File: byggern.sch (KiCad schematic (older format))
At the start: 41 parts, among them U1 ATmega162-16PU

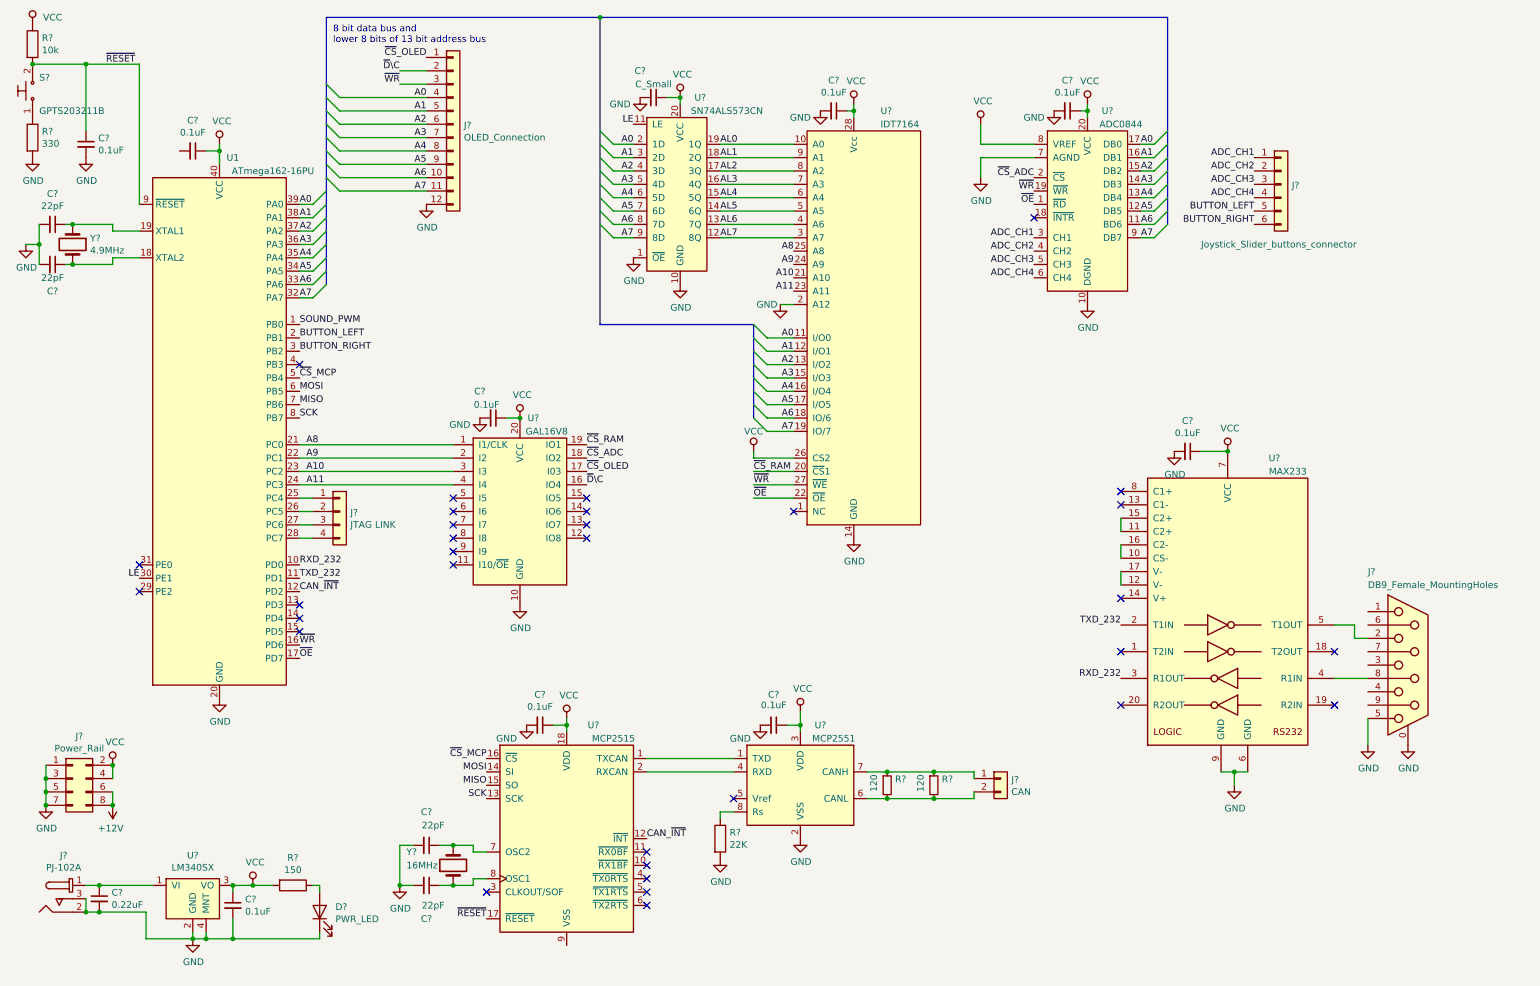
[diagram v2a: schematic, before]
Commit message: Correct warnings from electrical error check and change tri-state to output rule to ignore, no critical warnings left
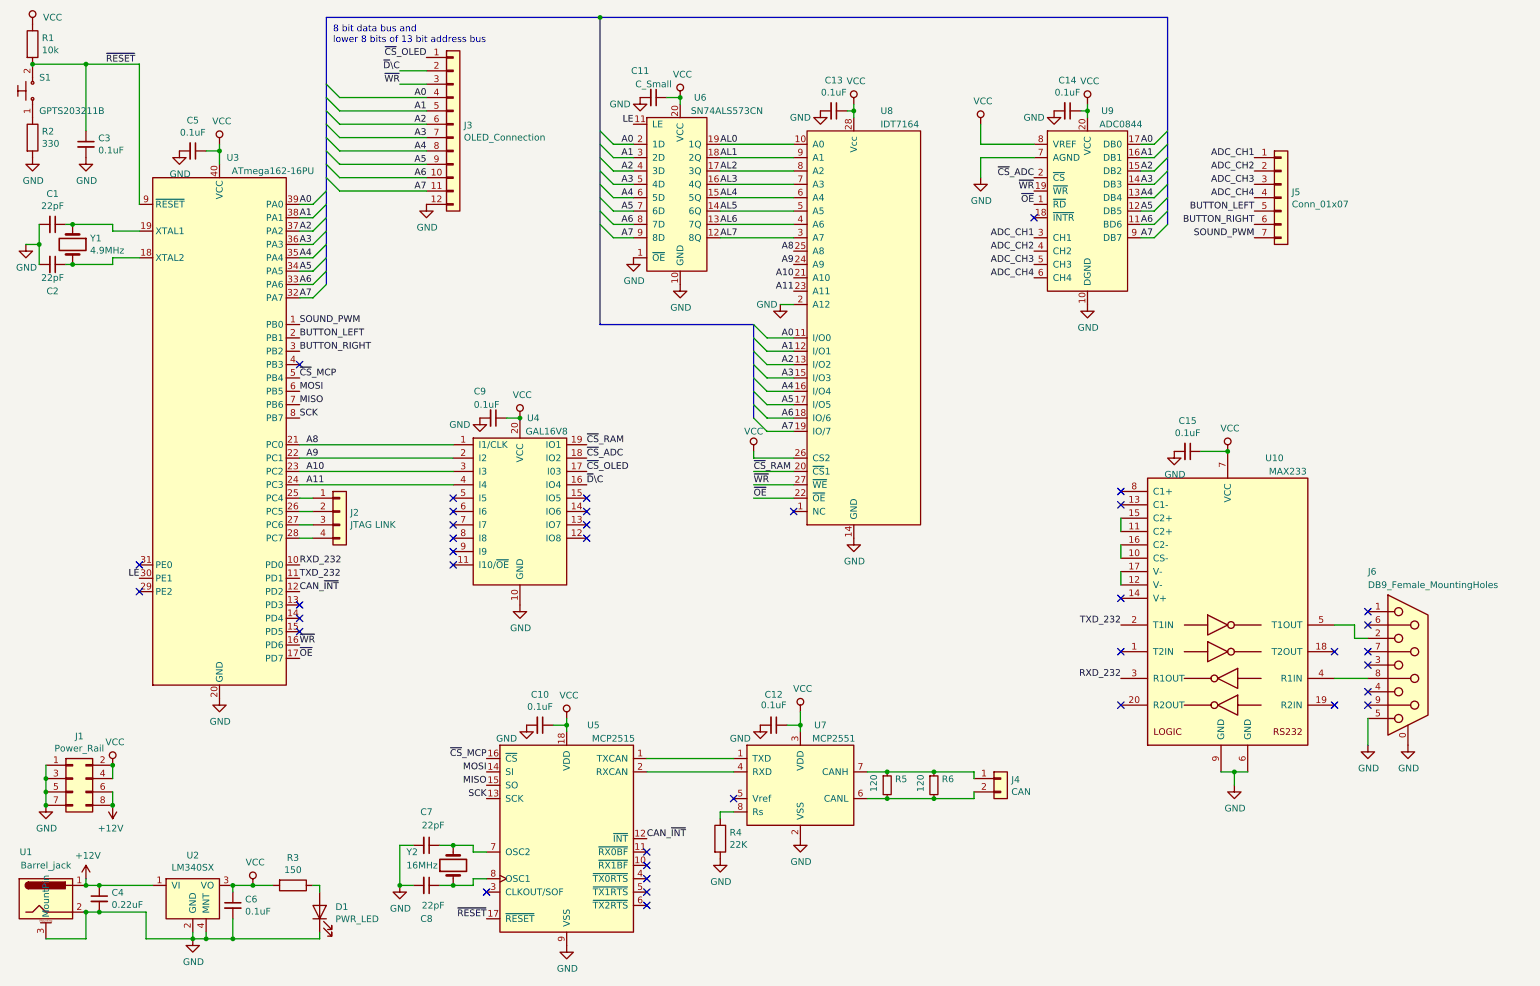
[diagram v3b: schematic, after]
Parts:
- removed J?: PJ-102A, digikey-footprints:Barrel_Jack_5.5mmODx2.1mmID_PJ-102A, symbol dk_Barrel-Power-Connectors:PJ-102A
- removed J?: Joystick_Slider_buttons_connector, symbol Connector_Generic:Conn_01x06
- added J5: Conn_01x07, symbol Connector_Generic:Conn_01x07
- added U1: Barrel_jack, symbol byggern:Barrel_jack
- gave numbers to parts that had none: 38
- renumbered U1 to U3
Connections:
- net +12V: now also C4.1, U2.1 (VI), U1.1
- net ADC_CH1: now also J5.1 (Pin_1)
- net ADC_CH2: now also J5.2 (Pin_2)
- net ADC_CH3: now also J5.3 (Pin_3)
- net ADC_CH4: now also J5.4 (Pin_4)
- net BUTTON_LEFT: now also J5.5 (Pin_5)
- net BUTTON_RIGHT: now also J5.6 (Pin_6)
- net GND: now also C5.2, U5.9 (VSS), U1.2, U1.3 (MountPin)
- net SOUND_PWM: now also J5.7 (Pin_7)
- no-connect marks 32 -> 38

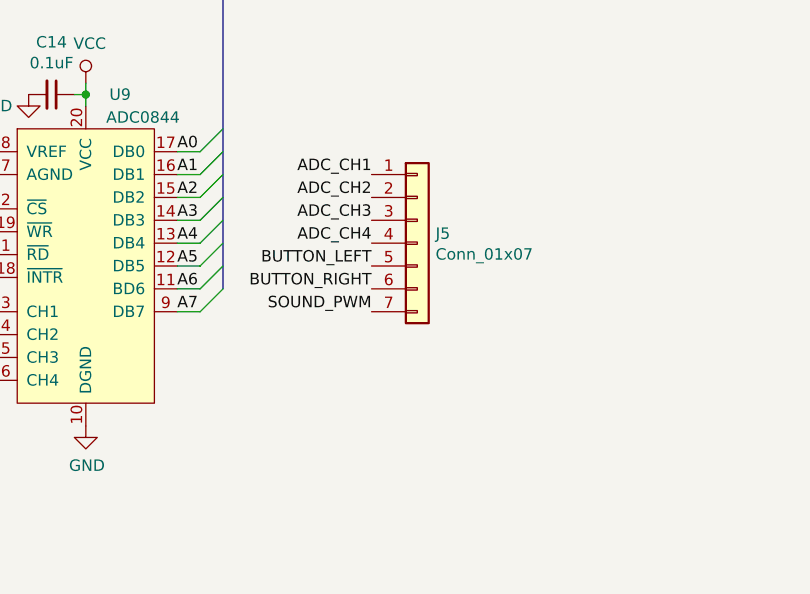
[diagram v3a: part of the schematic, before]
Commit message: Correct error in gitignore and add power to P1000-header
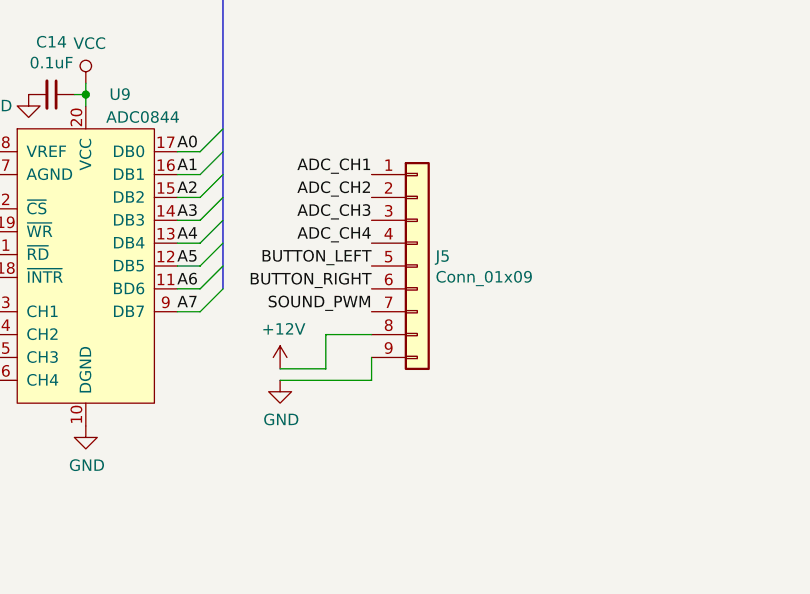
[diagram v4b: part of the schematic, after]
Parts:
- removed J5: Conn_01x07, symbol Connector_Generic:Conn_01x07
- added J5: Conn_01x09, symbol Connector_Generic:Conn_01x09
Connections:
- net +12V: now also J5.8 (Pin_8)
- net ADC_CH1: now also J5.1 (Pin_1)
- net ADC_CH2: now also J5.2 (Pin_2)
- net ADC_CH3: now also J5.3 (Pin_3)
- net ADC_CH4: now also J5.4 (Pin_4)
- net BUTTON_LEFT: now also J5.5 (Pin_5)
- net BUTTON_RIGHT: now also J5.6 (Pin_6)
- net GND: now also J5.9 (Pin_9)
- net SOUND_PWM: now also J5.7 (Pin_7)
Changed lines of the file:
@@
 	10450 5500 10700 5500
 $Comp
-L power:GND #PWR043
+L power:GND #PWR045
 U 1 1 5D9F4210
 P 10700 6000
-F 0 "#PWR043" H 10700 5750 50  0001 C CNN
+F 0 "#PWR045" H 10700 5750 50  0001 C CNN
 F 1 "GND" H 10705 5827 50  0000 C CNN
 F 2 "" H 10700 6000 50  0001 C CNN
@@
 $EndComp
 $Comp
-L power:GND #PWR044
+L power:GND #PWR046
 U 1 1 5D9F4B68
 P 11000 6000
-F 0 "#PWR044" H 11000 5750 50  0001 C CNN
+F 0 "#PWR046" H 11000 5750 50  0001 C CNN
 F 1 "GND" H 11005 5827 50  0000 C CNN
 F 2 "" H 11000 6000 50  0001 C CNN
@@
 	9700 6200 9600 6200
 $Comp
-L power:GND #PWR042
+L power:GND #PWR044
 U 1 1 5DA02D2F
 P 9700 6300
-F 0 "#PWR042" H 9700 6050 50  0001 C CNN
+F 0 "#PWR044" H 9700 6050 50  0001 C CNN
 F 1 "GND" H 9705 6127 50  0000 C CNN
 F 2 "" H 9700 6300 50  0001 C CNN
@@
 $EndComp
 $Comp
-L power:VCC #PWR041
+L power:VCC #PWR043
 U 1 1 5D9E6B36
 P 9650 3800
-F 0 "#PWR041" H 9650 3650 50  0001 C CNN
+F 0 "#PWR043" H 9650 3650 50  0001 C CNN
 F 1 "VCC" H 9667 3973 50  0000 C CNN
 F 2 "" H 9650 3800 50  0001 C CNN
@@
 	1    0    0    -1
 $EndComp
-$Comp
-L Connector_Generic:Conn_01x07 J5
-U 1 1 5DF07C49
-P 10050 1900
-F 0 "J5" H 10130 1942 50  0000 L CNN
-F 1 "Conn_01x07" H 10130 1851 50  0000 L CNN
-F 2 "" H 10050 1900 50  0001 C CNN
-F 3 "~" H 10050 1900 50  0001 C CNN
-	1    10050 1900
-	1    0    0    -1
-$EndComp
 Text Label 9850 2200 2    50   ~ 0
 SOUND_PWM
+$Comp
+L Connector_Generic:Conn_01x09 J5
+U 1 1 5D9EFB95
+P 10050 2000
+F 0 "J5" H 10130 2042 50  0000 L CNN
+F 1 "Conn_01x09" H 10130 1951 50  0000 L CNN
+F 2 "" H 10050 2000 50  0001 C CNN
+F 3 "~" H 10050 2000 50  0001 C CNN
+	1    10050 2000
+	1    0    0    -1
+$EndComp
+Wire Wire Line
+	9850 2300 9650 2300
+Wire Wire Line
+	9850 2400 9850 2500
+Wire Wire Line
+	9850 2500 9450 2500
+$Comp
+L power:GND #PWR042
+U 1 1 5DA033E3
+P 9450 2500
+F 0 "#PWR042" H 9450 2250 50  0001 C CNN
+F 1 "GND" H 9455 2327 50  0000 C CNN
+F 2 "" H 9450 2500 50  0001 C CNN
+F 3 "" H 9450 2500 50  0001 C CNN
+	1    9450 2500
+	1    0    0    -1
+$EndComp
+$Comp
+L power:+12V #PWR041
+U 1 1 5DA06A7C
+P 9450 2450
+F 0 "#PWR041" H 9450 2300 50  0001 C CNN
+F 1 "+12V" H 9465 2623 50  0000 C CNN
+F 2 "" H 9450 2450 50  0001 C CNN
+F 3 "" H 9450 2450 50  0001 C CNN
+	1    9450 2450
+	1    0    0    -1
+$EndComp
+Wire Wire Line
+	9650 2300 9650 2450
+Wire Wire Line
+	9650 2450 9450 2450
 Wire Bus Line
 	6100 2850 6100 3550

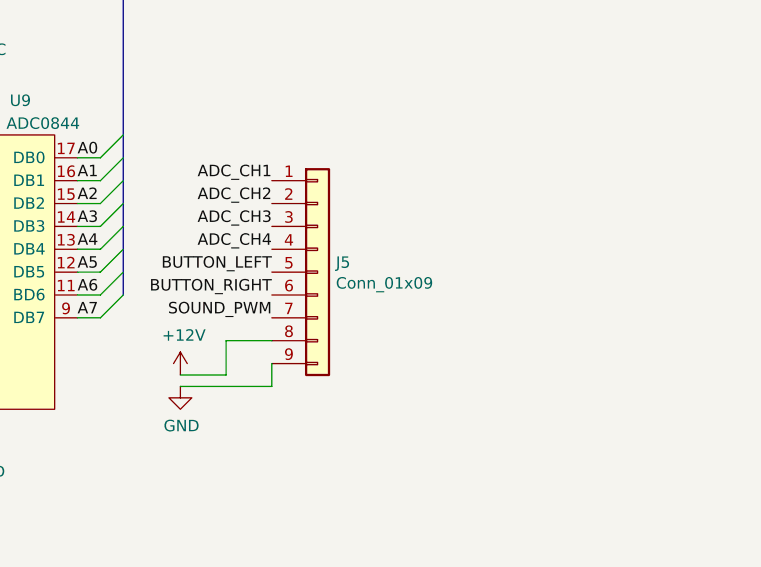
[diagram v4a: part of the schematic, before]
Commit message: Change name of P1000 Header
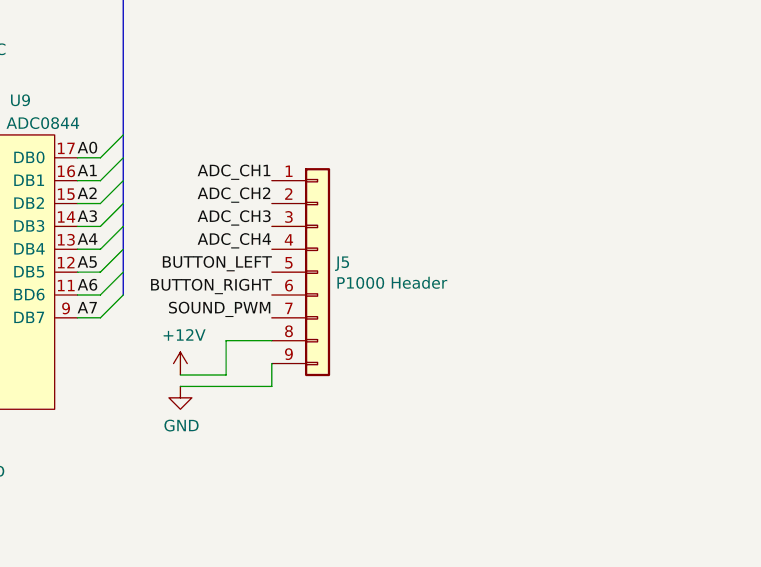
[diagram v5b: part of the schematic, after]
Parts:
- J5: value Conn_01x09 -> P1000 Header
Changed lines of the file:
@@
 P 10050 2000
 F 0 "J5" H 10130 2042 50  0000 L CNN
-F 1 "Conn_01x09" H 10130 1951 50  0000 L CNN
+F 1 "P1000 Header" H 10130 1951 50  0000 L CNN
 F 2 "" H 10050 2000 50  0001 C CNN
 F 3 "~" H 10050 2000 50  0001 C CNN

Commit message: Start assignment of footprints
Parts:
- C1, C10, C11, C12, C13, C14, C15, C2, C3, C4, C5, C6, C7, C8, C9: footprint (none) -> Capacitor_SMD:C_0805_2012Metric_Pad1.15x1.40mm_HandSolder
- J1: footprint (none) -> Connector_PinHeader_2.54mm:PinHeader_2x04_P2.54mm_Vertical
- J2: footprint (none) -> Connector_PinHeader_2.54mm:PinHeader_1x04_P2.54mm_Vertical
- J3: footprint (none) -> Connector_PinHeader_2.54mm:PinHeader_1x12_P2.54mm_Vertical
- J4: footprint (none) -> Connector_PinHeader_2.54mm:PinHeader_1x02_P2.54mm_Vertical
- J5: footprint (none) -> Connector_PinHeader_2.54mm:PinHeader_1x09_P2.54mm_Vertical
- R1, R2, R3, R4, R5, R6: footprint (none) -> Resistor_SMD:R_0805_2012Metric_Pad1.15x1.40mm_HandSolder
- U1: footprint (none) -> Connector_BarrelJack:BarrelJack_Horizontal
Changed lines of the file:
@@
 F 0 "C6" H 2292 7246 50  0000 L CNN
 F 1 "0.1uF" H 2292 7155 50  0000 L CNN
-F 2 "" H 2200 7200 50  0001 C CNN
+F 2 "Capacitor_SMD:C_0805_2012Metric_Pad1.15x1.40mm_HandSolder" H 2200 7200 50  0001 C CNN
 F 3 "~" H 2200 7200 50  0001 C CNN
 	1    2200 7200
@@
 F 0 "R3" V 2443 7050 50  0000 C CNN
 F 1 "150" V 2534 7050 50  0000 C CNN
-F 2 "" V 2580 7050 50  0001 C CNN
+F 2 "Resistor_SMD:R_0805_2012Metric_Pad1.15x1.40mm_HandSolder" V 2580 7050 50  0001 C CNN
 F 3 "~" H 2650 7050 50  0001 C CNN
 	1    2650 7050
@@
 F 0 "J1" H 1050 6567 50  0000 C CNN
 F 1 "Power_Rail" H 1050 6476 50  0000 C CNN
-F 2 "" H 1000 6250 50  0001 C CNN
+F 2 "Connector_PinHeader_2.54mm:PinHeader_2x04_P2.54mm_Vertical" H 1000 6250 50  0001 C CNN
 F 3 "~" H 1000 6250 50  0001 C CNN
 	1    1000 6250
@@
 F 0 "C1" V 621 2100 50  0000 C CNN
 F 1 "22pF" V 712 2100 50  0000 C CNN
-F 2 "" H 850 2100 50  0001 C CNN
+F 2 "Capacitor_SMD:C_0805_2012Metric_Pad1.15x1.40mm_HandSolder" H 850 2100 50  0001 C CNN
 F 3 "~" H 850 2100 50  0001 C CNN
 	1    850  2100
@@
 F 0 "C2" V 1050 2400 50  0000 C CNN
 F 1 "22pF" V 950 2400 50  0000 C CNN
-F 2 "" H 850 2400 50  0001 C CNN
+F 2 "Capacitor_SMD:C_0805_2012Metric_Pad1.15x1.40mm_HandSolder" H 850 2400 50  0001 C CNN
 F 3 "~" H 850 2400 50  0001 C CNN
 	1    850  2400
@@
 F 0 "R1" H 770 796 50  0000 L CNN
 F 1 "10k" H 770 705 50  0000 L CNN
-F 2 "" V 630 750 50  0001 C CNN
+F 2 "Resistor_SMD:R_0805_2012Metric_Pad1.15x1.40mm_HandSolder" V 630 750 50  0001 C CNN
 F 3 "~" H 700 750 50  0001 C CNN
 	1    700  750
@@
 F 0 "R2" H 770 1496 50  0000 L CNN
 F 1 "330" H 770 1405 50  0000 L CNN
-F 2 "" V 630 1450 50  0001 C CNN
+F 2 "Resistor_SMD:R_0805_2012Metric_Pad1.15x1.40mm_HandSolder" V 630 1450 50  0001 C CNN
 F 3 "~" H 700 1450 50  0001 C CNN
 	1    700  1450
@@
 F 0 "C3" H 1192 1546 50  0000 L CNN
 F 1 "0.1uF" H 1192 1455 50  0000 L CNN
-F 2 "" H 1100 1500 50  0001 C CNN
+F 2 "Capacitor_SMD:C_0805_2012Metric_Pad1.15x1.40mm_HandSolder" H 1100 1500 50  0001 C CNN
 F 3 "~" H 1100 1500 50  0001 C CNN
 	1    1100 1500
@@
 F 0 "J2" H 3080 4242 50  0000 L CNN
 F 1 "JTAG LINK" H 3080 4151 50  0000 L CNN
-F 2 "" H 3000 4250 50  0001 C CNN
+F 2 "Connector_PinHeader_2.54mm:PinHeader_1x04_P2.54mm_Vertical" H 3000 4250 50  0001 C CNN
 F 3 "~" H 3000 4250 50  0001 C CNN
 	1    3000 4250
@@
 F 0 "C15" V 9121 3800 50  0000 C CNN
 F 1 "0.1uF" V 9212 3800 50  0000 C CNN
-F 2 "" H 9350 3800 50  0001 C CNN
+F 2 "Capacitor_SMD:C_0805_2012Metric_Pad1.15x1.40mm_HandSolder" H 9350 3800 50  0001 C CNN
 F 3 "~" H 9350 3800 50  0001 C CNN
 	1    9350 3800
@@
 F 0 "J3" H 3930 1342 50  0000 L CNN
 F 1 "OLED_Connection" H 3930 1251 50  0000 L CNN
-F 2 "" H 3850 1350 50  0001 C CNN
+F 2 "Connector_PinHeader_2.54mm:PinHeader_1x12_P2.54mm_Vertical" H 3850 1350 50  0001 C CNN
 F 3 "~" H 3850 1350 50  0001 C CNN
 	1    3850 1350
@@
 F 0 "C9" V 3950 3450 50  0000 C CNN
 F 1 "0.1uF" V 4050 3500 50  0000 C CNN
-F 2 "" H 4150 3550 50  0001 C CNN
+F 2 "Capacitor_SMD:C_0805_2012Metric_Pad1.15x1.40mm_HandSolder" H 4150 3550 50  0001 C CNN
 F 3 "~" H 4150 3550 50  0001 C CNN
 	1    4150 3550
@@
 F 0 "C13" V 6471 1250 50  0000 C CNN
 F 1 "0.1uF" V 6562 1250 50  0000 C CNN
-F 2 "" H 6700 1250 50  0001 C CNN
+F 2 "Capacitor_SMD:C_0805_2012Metric_Pad1.15x1.40mm_HandSolder" H 6700 1250 50  0001 C CNN
 F 3 "~" H 6700 1250 50  0001 C CNN
 	1    6700 1250
@@
 F 0 "C11" V 5150 1050 50  0000 C CNN
 F 1 "C_Small" V 5250 1150 50  0000 C CNN
-F 2 "" H 5350 1150 50  0001 C CNN
+F 2 "Capacitor_SMD:C_0805_2012Metric_Pad1.15x1.40mm_HandSolder" H 5350 1150 50  0001 C CNN
 F 3 "~" H 5350 1150 50  0001 C CNN
 	1    5350 1150
@@
 F 0 "C14" V 8221 1250 50  0000 C CNN
 F 1 "0.1uF" V 8312 1250 50  0000 C CNN
-F 2 "" H 8450 1250 50  0001 C CNN
+F 2 "Capacitor_SMD:C_0805_2012Metric_Pad1.15x1.40mm_HandSolder" H 8450 1250 50  0001 C CNN
 F 3 "~" H 8450 1250 50  0001 C CNN
 	1    8450 1250
@@
 F 0 "C5" V 1671 1550 50  0000 C CNN
 F 1 "0.1uF" V 1762 1550 50  0000 C CNN
-F 2 "" H 1900 1550 50  0001 C CNN
+F 2 "Capacitor_SMD:C_0805_2012Metric_Pad1.15x1.40mm_HandSolder" H 1900 1550 50  0001 C CNN
 F 3 "~" H 1900 1550 50  0001 C CNN
 	1    1900 1550
@@
 F 0 "C7" V 3400 6750 50  0000 C CNN
 F 1 "22pF" V 3500 6800 50  0000 C CNN
-F 2 "" H 3650 6750 50  0001 C CNN
+F 2 "Capacitor_SMD:C_0805_2012Metric_Pad1.15x1.40mm_HandSolder" H 3650 6750 50  0001 C CNN
 F 3 "~" H 3650 6750 50  0001 C CNN
 	1    3650 6750
@@
 F 0 "C8" V 3900 7050 50  0000 C CNN
 F 1 "22pF" V 3800 7100 50  0000 C CNN
-F 2 "" H 3650 7050 50  0001 C CNN
+F 2 "Capacitor_SMD:C_0805_2012Metric_Pad1.15x1.40mm_HandSolder" H 3650 7050 50  0001 C CNN
 F 3 "~" H 3650 7050 50  0001 C CNN
 	1    3650 7050
@@
 F 0 "C10" V 4271 5850 50  0000 C CNN
 F 1 "0.1uF" V 4362 5850 50  0000 C CNN
-F 2 "" H 4500 5850 50  0001 C CNN
+F 2 "Capacitor_SMD:C_0805_2012Metric_Pad1.15x1.40mm_HandSolder" H 4500 5850 50  0001 C CNN
 F 3 "~" H 4500 5850 50  0001 C CNN
 	1    4500 5850
@@
 F 0 "C12" V 6021 5850 50  0000 C CNN
 F 1 "0.1uF" V 6100 5850 50  0000 C CNN
-F 2 "" H 6250 5850 50  0001 C CNN
+F 2 "Capacitor_SMD:C_0805_2012Metric_Pad1.15x1.40mm_HandSolder" H 6250 5850 50  0001 C CNN
 F 3 "~" H 6250 5850 50  0001 C CNN
 	1    6250 5850
@@
 F 0 "R4" H 5920 6746 50  0000 L CNN
 F 1 "22K" H 5920 6655 50  0000 L CNN
-F 2 "" V 5780 6700 50  0001 C CNN
+F 2 "Resistor_SMD:R_0805_2012Metric_Pad1.15x1.40mm_HandSolder" V 5780 6700 50  0001 C CNN
 F 3 "~" H 5850 6700 50  0001 C CNN
 	1    5850 6700
@@
 F 0 "R5" H 7159 6346 50  0000 L CNN
 F 1 "120" V 7000 6250 50  0000 L CNN
-F 2 "" H 7100 6300 50  0001 C CNN
+F 2 "Resistor_SMD:R_0805_2012Metric_Pad1.15x1.40mm_HandSolder" H 7100 6300 50  0001 C CNN
 F 3 "~" H 7100 6300 50  0001 C CNN
 	1    7100 6300
@@
 F 0 "R6" H 7509 6346 50  0000 L CNN
 F 1 "120" V 7350 6250 50  0000 L CNN
-F 2 "" H 7450 6300 50  0001 C CNN
+F 2 "Resistor_SMD:R_0805_2012Metric_Pad1.15x1.40mm_HandSolder" H 7450 6300 50  0001 C CNN
 F 3 "~" H 7450 6300 50  0001 C CNN
 	1    7450 6300
@@
 F 0 "J4" H 8030 6242 50  0000 L CNN
 F 1 "CAN" H 8030 6151 50  0000 L CNN
-F 2 "" H 7950 6250 50  0001 C CNN
+F 2 "Connector_PinHeader_2.54mm:PinHeader_1x02_P2.54mm_Vertical" H 7950 6250 50  0001 C CNN
 F 3 "~" H 7950 6250 50  0001 C CNN
 	1    7950 6250
@@
 F 0 "C4" H 1292 7196 50  0000 L CNN
 F 1 "0.22uF" H 1292 7105 50  0000 L CNN
-F 2 "" H 1200 7150 50  0001 C CNN
+F 2 "Capacitor_SMD:C_0805_2012Metric_Pad1.15x1.40mm_HandSolder" H 1200 7150 50  0001 C CNN
 F 3 "~" H 1200 7150 50  0001 C CNN
 	1    1200 7150
@@
 F 0 "U1" H 650 6800 50  0000 C CNN
 F 1 "Barrel_jack" H 800 6700 50  0000 C CNN
-F 2 "" H 750 6800 50  0001 C CNN
+F 2 "Connector_BarrelJack:BarrelJack_Horizontal" H 750 6800 50  0001 C CNN
 F 3 "" H 750 6800 50  0001 C CNN
 	1    750  6800
@@
 F 0 "J5" H 10130 2042 50  0000 L CNN
 F 1 "P1000 Header" H 10130 1951 50  0000 L CNN
-F 2 "" H 10050 2000 50  0001 C CNN
+F 2 "Connector_PinHeader_2.54mm:PinHeader_1x09_P2.54mm_Vertical" H 10050 2000 50  0001 C CNN
 F 3 "~" H 10050 2000 50  0001 C CNN
 	1    10050 2000
